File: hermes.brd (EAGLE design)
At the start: 100 x 80 mm, 36 parts, among them IC1 MIC5219-3.3BML

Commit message: -Update Library -Correct P2P pins -Place general position of components
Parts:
- moved CONN1 87.6 mm to (6.35, 45.7), turned to 270 degrees
- moved CONN2 86.4 mm to (91.4, 45.7), turned to 90 degrees
- moved R2 56.4 mm to (50.8, 8.89), turned to 180 degrees
- moved R1 56.4 mm to (29.2, 19.1), turned to 270 degrees
- moved LED1 56.4 mm to (29.2, 16.5), turned to 90 degrees
- moved R7 56.2 mm to (45.7, 8.89), turned to 180 degrees
- moved R3 56.1 mm to (49.5, 8.89), turned to 180 degrees
- moved R6 56.0 mm to (47.0, 8.89), turned to 180 degrees
- moved R5 55.9 mm to (48.3, 8.89), turned to 180 degrees
- moved TP2 55.7 mm to (29.2, 22.9)
- moved TP3 50.3 mm to (20.3, 33.0)
- moved L1 32.9 mm to (44.5, 30.5), turned to 270 degrees
- moved C6 30.9 mm to (44.5, 29.2), turned to 270 degrees
- moved TP1 25.8 mm to (14.0, 47.6)
- moved C5 24.7 mm to (49.5, 35.6), turned to 180 degrees
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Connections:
- net +3V3: no longer IC1.P$7
- net GND: now also CONN2.P$5, IC1.P$7; no longer CONN2.P$4
- net SERCOM5_SCL: now also CONN2.P$3; no longer CONN2.P$6
- net SERCOM5_SDA: now also CONN2.P$4; no longer CONN2.P$5
- net VCC: now also CONN2.P$6; no longer CONN2.P$3
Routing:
- net GND: track 0.00 -> 3.60 mm

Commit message: -General routing
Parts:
- moved PIN11 47.7 mm to (49.5, 44.5), turned to 90 degrees
- moved PIN12 46.0 mm to (50.8, 44.5), turned to 90 degrees
- moved PIN13 44.4 mm to (52.1, 44.5), turned to 90 degrees
- moved PIN10 42.7 mm to (55.9, 44.5), turned to 90 degrees
- moved PIN14 42.7 mm to (53.3, 44.5), turned to 90 degrees
- moved PIN9 41.0 mm to (54.6, 44.5), turned to 90 degrees
- moved TP1 36.8 mm to (50.8, 47.6)
- moved TP3 36.6 mm to (50.8, 53.3)
- moved R1 17.0 mm to (44.5, 26.7)
- moved LED1 17.0 mm to (44.5, 24.1)
- moved LED2 17.0 mm to (43.2, 24.1)
- moved R4 17.0 mm to (43.2, 26.7)
- moved C2 16.7 mm to (57.1, 21.6), turned to 180 degrees
- moved C3 16.7 mm to (59.7, 24.1), turned to 0 degrees
- moved XTAL1 16.5 mm to (58.4, 22.9), turned to 0 degrees
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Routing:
- net VCC: track 0.00 -> 109.1 mm, vias 0 -> 3
- net SERCOM5_SDA: track 0.00 -> 79.3 mm
- net SERCOM5_SCL: track 0.00 -> 79.3 mm
- net SERCOM_SCL: track 0.00 -> 55.4 mm, vias 0 -> 3
- net +3V3: track 0.00 -> 20.2 mm, vias 0 -> 9
- net !RESET: track 0.00 -> 11.7 mm, vias 0 -> 1
- net XOUT: track 0.00 -> 7.79 mm
- net XIN: track 0.00 -> 7.44 mm
- net N$1: track 0.00 -> 3.85 mm
- net LED: track 0.00 -> 3.07 mm
- net SERCOM0_SDA: track 0.00 -> 2.21 mm
- net SERCOM1_SDA: track 0.00 -> 2.20 mm
- net SERCOM2_SDA: track 0.00 -> 2.19 mm
- net SERCOM4_SDA: track 0.00 -> 2.18 mm
- net SERCOM3_SDA: track 0.00 -> 2.18 mm
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- added copper zone on layer 2, net +3V3
- added copper zone on layer 16, net GND

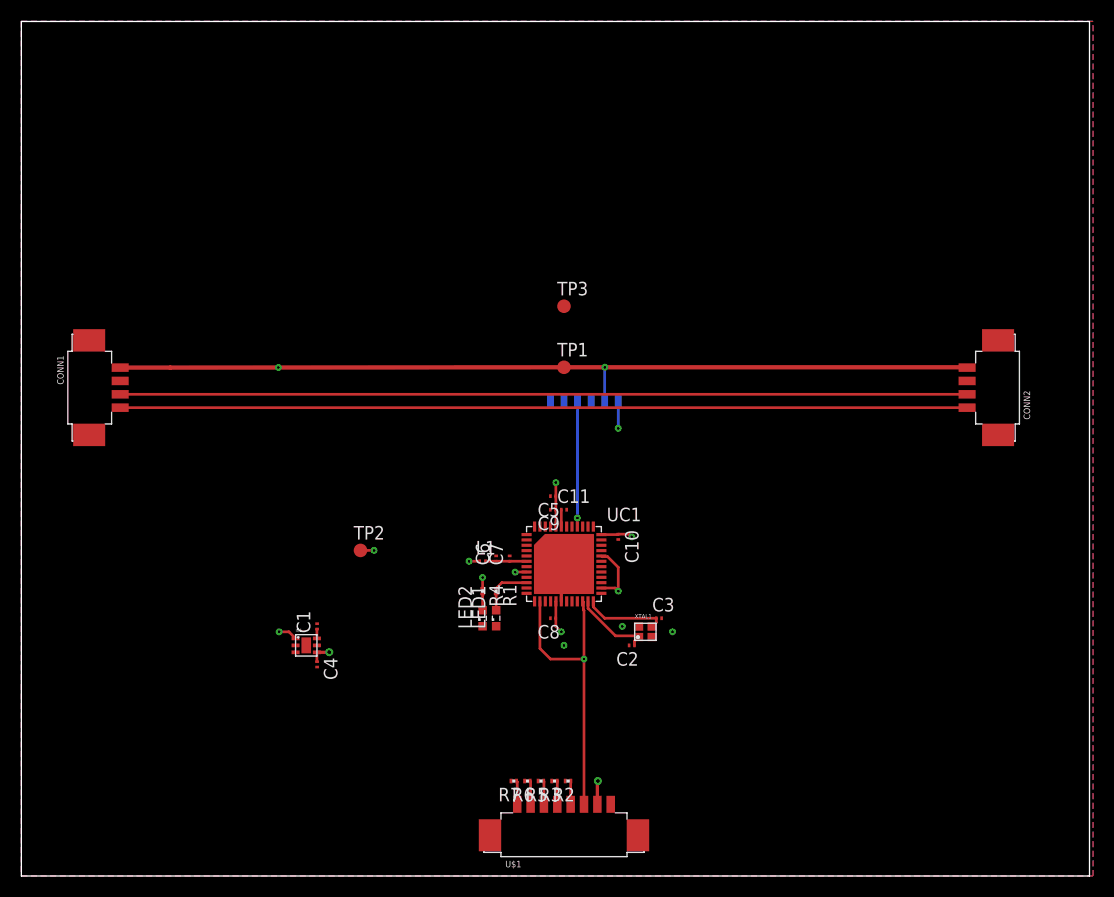
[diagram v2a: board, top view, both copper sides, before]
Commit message: MIniaturization of board process
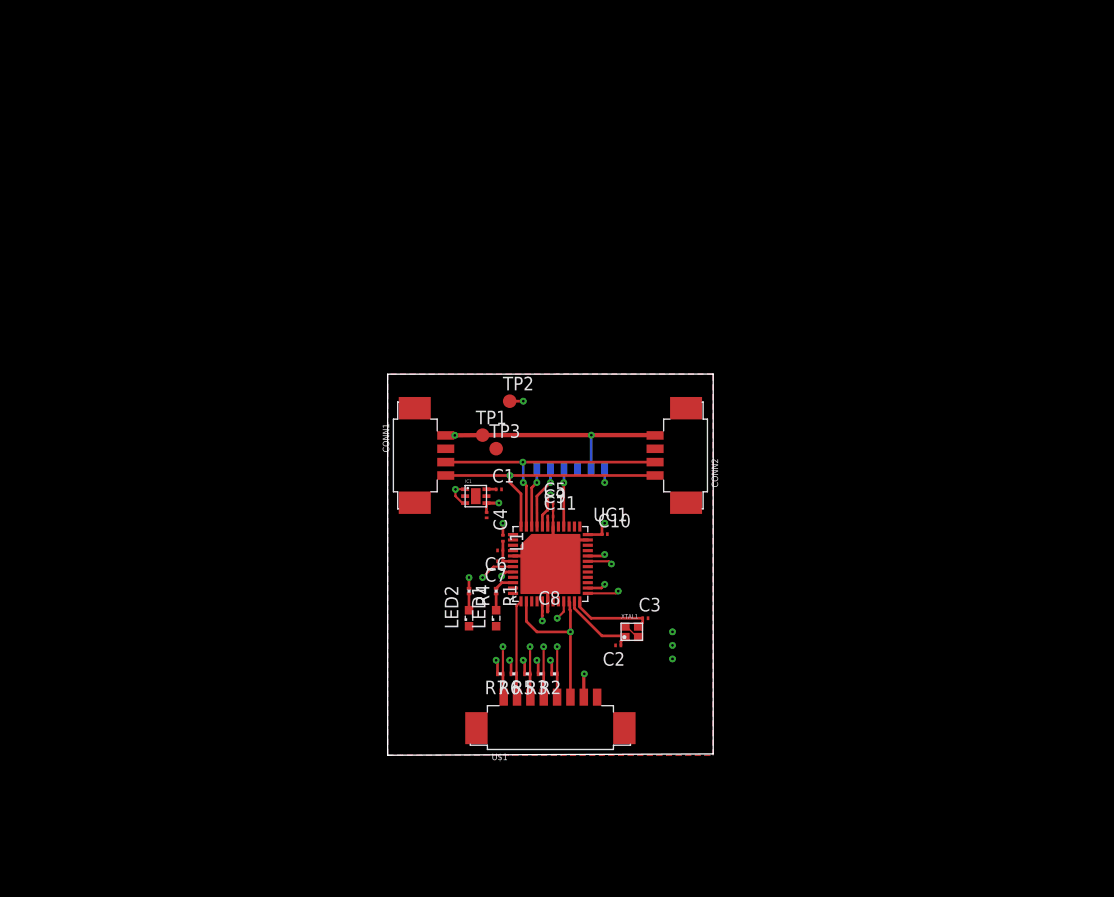
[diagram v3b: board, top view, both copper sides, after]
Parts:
- moved CONN1 31.1 mm to (36.8, 39.4)
- moved CONN2 29.9 mm to (62.2, 39.4)
- moved C1 21.3 mm to (44.7, 36.2), turned to 0 degrees
- moved IC1 21.1 mm to (42.5, 35.6)
- moved C4 21.1 mm to (43.6, 33.8)
- moved TP2 19.8 mm to (45.7, 44.5)
- moved TP3 14.8 mm to (44.5, 40.0)
- moved U$1 10.1 mm to (49.5, 13.8)
- moved R2 10.1 mm to (49.9, 18.9)
- moved R3 10.1 mm to (48.6, 18.9)
- moved R5 10.1 mm to (47.4, 18.9)
- moved R6 10.1 mm to (46.1, 18.9)
- moved R7 10.1 mm to (44.8, 18.9)
- moved TP1 9.92 mm to (43.2, 41.3)
- moved PIN10 6.48 mm to (54.6, 38.1)
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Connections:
- net SERCOM0_SDA: now also R6.1, U$1.P$4; no longer R7.1, U$1.P$3
- net SERCOM1_SDA: now also R2.1, U$1.P$7; no longer R6.1, U$1.P$4
- net SERCOM4_SDA: now also R7.1, U$1.P$3; no longer R2.1, U$1.P$7
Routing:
- net VCC: track 109.1 -> 30.7 mm
- net SERCOM5_SCL: track 79.3 -> 24.8 mm, vias 0 -> 1
- net SERCOM5_SDA: track 79.3 -> 25.8 mm, vias 0 -> 2
- net SERCOM3_SDA: track 2.18 -> 20.3 mm, vias 0 -> 2
- net GND: track 3.60 -> 20.3 mm
- net SERCOM_SCL: track 55.4 -> 38.7 mm, vias 3 -> 4
- net SERCOM1_SDA: track 2.20 -> 17.8 mm, vias 0 -> 2
- net SERCOM4_SDA: track 2.18 -> 15.3 mm, vias 0 -> 2
- net SERCOM2_SDA: track 2.19 -> 10.7 mm, vias 0 -> 2
- net SERCOM0_SDA: track 2.21 -> 9.16 mm
- net !RESET: track 11.7 -> 5.40 mm
- net SWCLK: track 0.00 -> 5.92 mm, vias 0 -> 1
- net SWDIO: track 0.00 -> 5.59 mm, vias 0 -> 1
- net +3V3: track 20.2 -> 23.2 mm, vias 9 -> 14
- net LED: track 3.07 -> 1.80 mm
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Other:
- board size 100 x 80 mm -> 30.5 x 35.7 mm

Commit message: Reduction of board (Cont'd)
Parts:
- moved TP1 6.35 mm to (49.5, 41.3)
- moved C1 5.78 mm to (43.8, 30.5), turned to 270 degrees
- moved CONN2 5.08 mm to (57.1, 39.4)
- moved C3 4.38 mm to (54.6, 22.0), turned to 270 degrees
- moved C2 4.26 mm to (52.1, 23.5), turned to 270 degrees
- moved TP3 3.81 mm to (48.3, 40.0)
- moved XTAL1 3.81 mm to (53.3, 22.9), turned to 270 degrees
- moved C4 3.05 mm to (41.4, 31.6), turned to 180 degrees
- moved IC1 2.99 mm to (43.2, 32.6), turned to 270 degrees
- moved CONN1 2.54 mm to (39.4, 39.4)
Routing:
- net SERCOM5_SDA: track 25.8 -> 18.2 mm
- net SERCOM5_SCL: track 24.8 -> 17.2 mm
- net VCC: track 30.7 -> 25.5 mm
- net XIN: track 7.44 -> 2.97 mm
- net XOUT: track 7.79 -> 5.68 mm
- net SERCOM_SCL: track 38.7 -> 39.9 mm
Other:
- board size 30.5 x 35.7 mm -> 22.9 x 35.1 mm

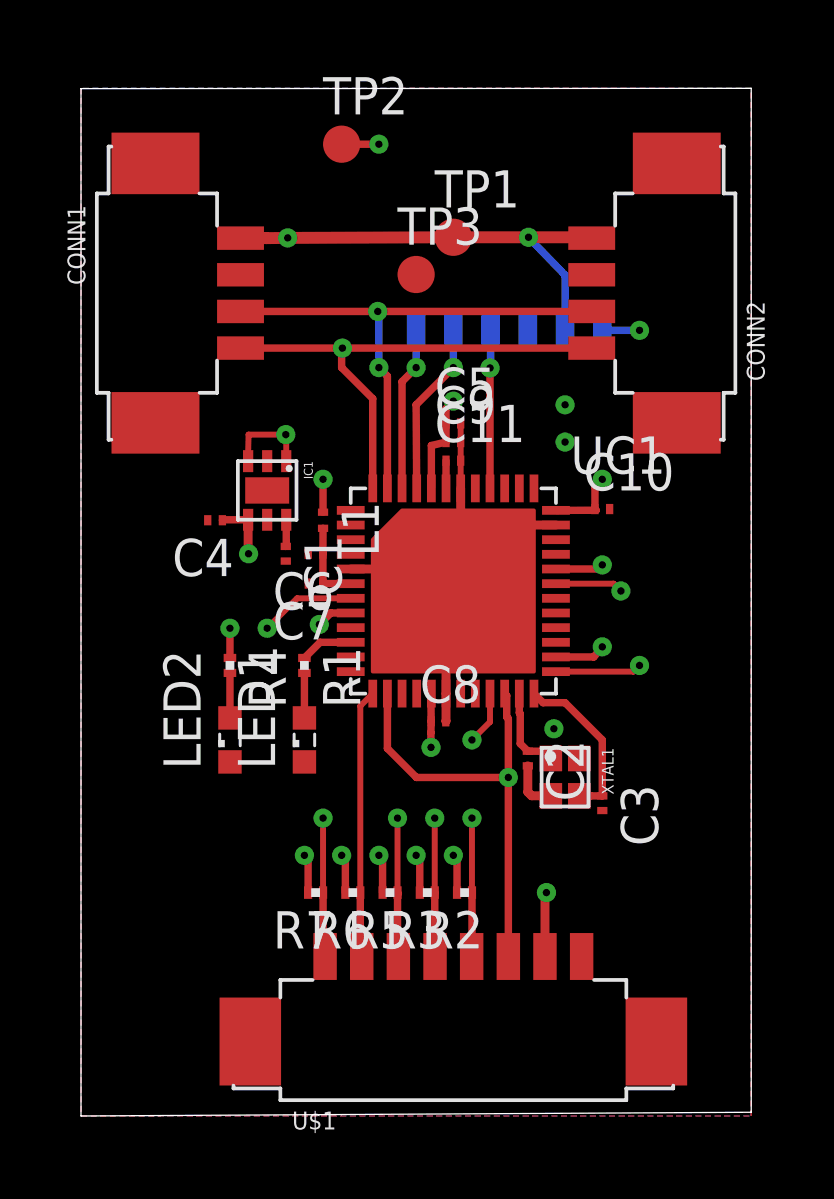
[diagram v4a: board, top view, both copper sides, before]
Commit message: First release of Hermes, Add Layout view and CAM files, Correct minor issues
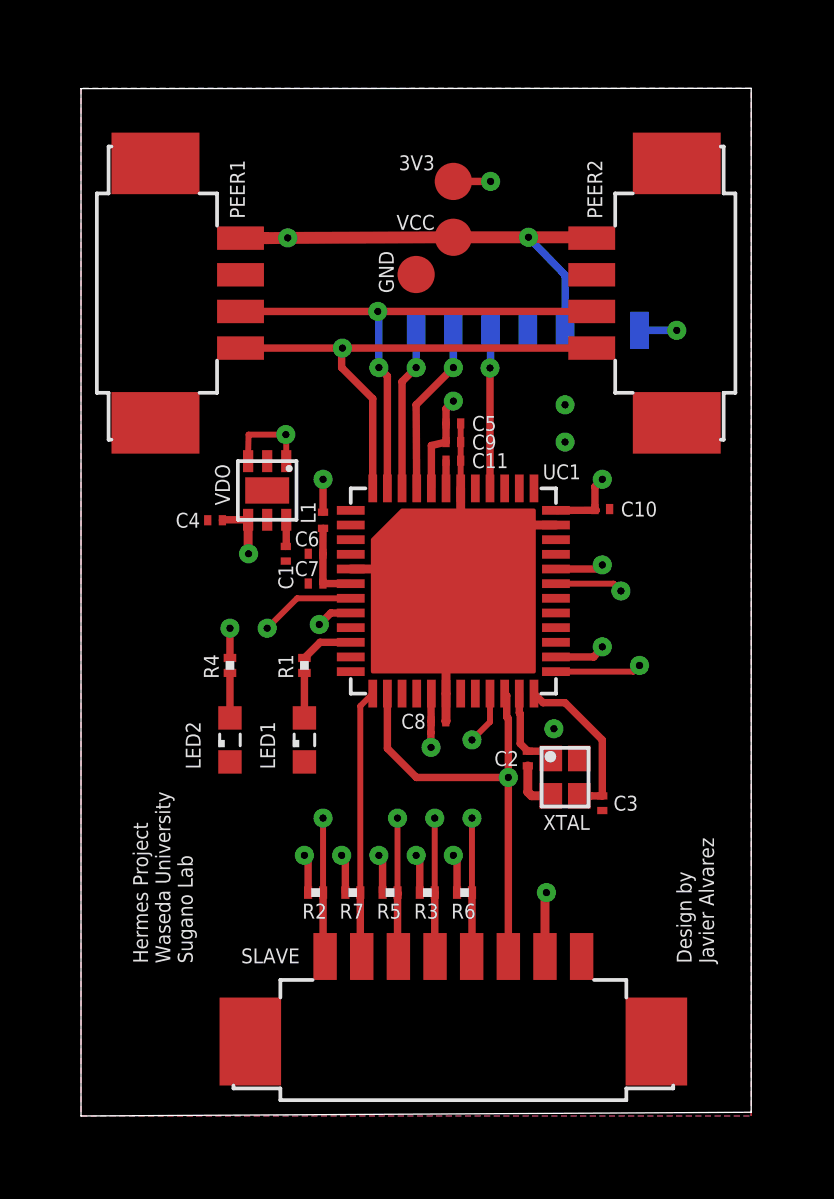
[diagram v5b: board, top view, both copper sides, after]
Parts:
- removed PIN10: SINGLE-PIN, Hermes_lib:PAD5025
- removed TP2: TPB1,27, testpad:B1,27
- added 3V3: TPB1,27, testpad:B1,27
- added PIN2: SINGLE-PIN, Hermes_lib:PAD5025
- moved R2 5.08 mm to (44.8, 18.9)
- moved R6 3.81 mm to (49.9, 18.9)
- moved R7 1.27 mm to (46.1, 18.9)
- renumbered CONN1 to PEER1, CONN2 to PEER2, IC1 to VDO, PIN11 to PIN3, PIN12 to PIN4, PIN13 to PIN5, PIN14 to PIN6, PIN9 to PIN1, TP1 to VCC, TP3 to GND, U$1 to SLAVE, XTAL1 to XTAL
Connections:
- net +3V3: now also 3V3.TP, PIN2.P$1; no longer PIN10.P$1, TP2.TP
- net SERCOM0_SDA: now also R7.1; no longer R6.1
- net SERCOM1_SDA: now also R6.1; no longer R2.1
- net SERCOM4_SDA: now also R2.1; no longer R7.1
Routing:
- added copper zone on layer 15, net GND
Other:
- board text added: "Design by Javier Alvarez"
- board text added: "Hermes Project Waseda University Sugano Lab"

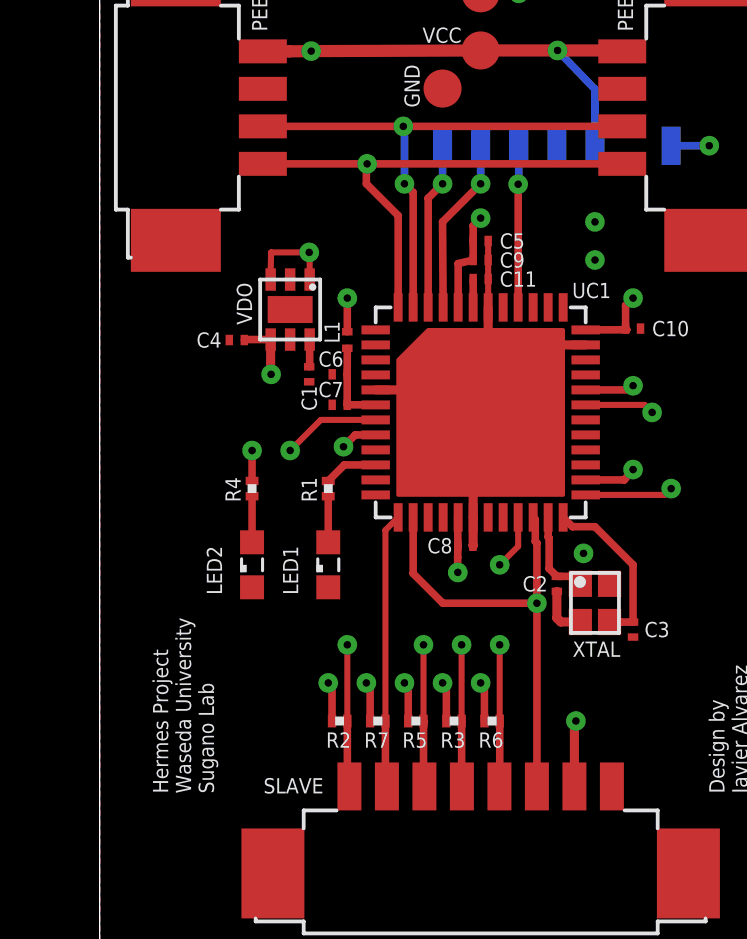
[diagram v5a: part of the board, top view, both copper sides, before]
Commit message: Replace components according to availability in digital stores (Capacitors and Inductors)
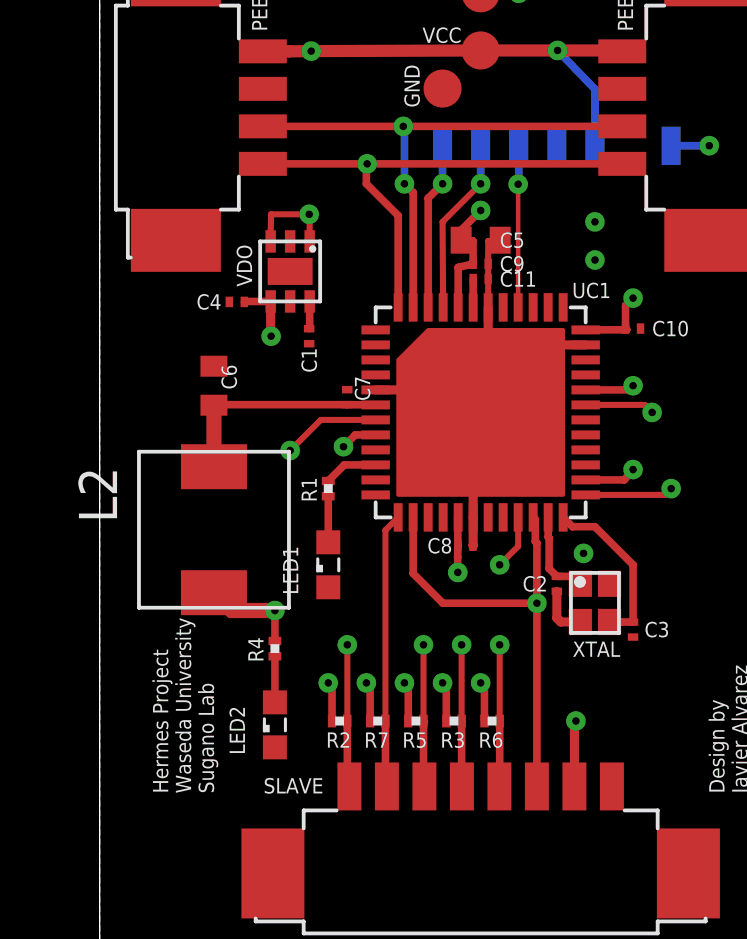
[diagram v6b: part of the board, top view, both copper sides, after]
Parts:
- removed L1: 10uH, rcl:L0201
- added L2: 10uH, Hermes_lib:L2215
- C5, C6: device rcl:C0201 -> rcl:C0402
- moved R4 5.39 mm to (42.7, 21.3)
- moved LED2 5.39 mm to (42.7, 18.8)
- moved C6 4.21 mm to (40.6, 30.1), turned to 90 degrees
- moved C1 1.27 mm to (43.8, 31.8)
- moved C4 1.27 mm to (41.4, 32.9)
- moved VDO 1.27 mm to (43.2, 33.9)
- moved C7 0.36 mm to (45.1, 29.7), turned to 90 degrees
- moved C9 0.13 mm to (49.5, 34.2)
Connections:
- net +3V3: now also L2.P$2; no longer L1.1
- net N$1: now also L2.P$1; no longer L1.2
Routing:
- net N$1: track 2.83 -> 7.45 mm
- net +3V3: track 23.4 -> 25.3 mm, vias 14 -> 13
- net VCC: track 25.5 -> 24.2 mm
